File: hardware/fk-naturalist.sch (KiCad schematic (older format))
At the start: 133 parts, among them J1 Conn_01x11, J10 S2B-PH-SM4-TB, J11 RF-SMA-EDGE, J2 Conn_01x05, J3 Conn_01x04, J5 Conn_01x03, J6 Conn_01x05, J7 CONN-HDR-2x5, J8 Conn_01x09, J9 MICRO-USB, M1 MOUNT_HOLE, M3 MOUNT_HOLE, M4 MOUNT_HOLE, M6 MOUNT_HOLE, M7 MICROSD, Q1 2N7002LT1G, Q2 2N7002LT1G, Q3 2N7002LT1G, Q4 2N7002LT1G, SW1 SPNO, SW2 SPNO, U1 ATWINC1500-MR210PA, U10 FGPMMOPA6H, U101 TSL2591, U102 MPL3115A2, U103 BNO055, U104 SHT31, U11 MAX1704XX, U2 ATSAMD21G18A-AU, U3 SPH0645, U4 24AA02E64, U5 S25FL116K0XMFI041, U6 BQ24074RGTT, U7 PCF8523, U8 MCP1700T-3302E/MB, U9 ISL8541x, Y1 FC-135, Y101 FC-135, Y2 FC-135

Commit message: Fix TSL2591 footprint.
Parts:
- U101: footprint Housings_DFN_QFN:DFN-6-1EP_2x2mm_Pitch0.65mm -> conservify:TSL2591
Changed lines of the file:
@@
 F 0 "U101" H 9150 15300 60  0000 C CNN
 F 1 "TSL2591" H 9150 15400 60  0000 C CNN
-F 2 "Housings_DFN_QFN:DFN-6-1EP_2x2mm_Pitch0.65mm" H 9150 15300 60  0001 C CNN
+F 2 "conservify:TSL2591" H 9150 15300 60  0001 C CNN
 F 3 "" H 9150 15300 60  0001 C CNN
 F 4 "0" H 9150 15400 50  0001 C CNN "price"

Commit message: More label/naming cleanup.
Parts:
- C10, C19, C20, C25: value 4.7uF 10V X5R -> 4.7uF
- C12: value 1uF 50V X5R -> 1uF
- C14: value 4.7nF 25V X7R -> 4.7nF
- C21, C23, C27, C29, C6: value 1uF 10V X5R -> 1uF
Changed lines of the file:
@@
 P 5550 1900
 F 0 "C6" V 5400 1850 50  0000 L CNN
-F 1 "1uF 10V X5R" V 5700 1650 50  0000 L CNN
+F 1 "1uF" V 5700 1650 50  0000 L CNN
 F 2 "RocketScreamKicadLibrary:CAP-0603" H 5550 1700 30  0001 C CNN
 F 3 "" H 5550 1900 60  0000 C CNN
@@
 P 9100 2500
 F 0 "C12" H 9250 2500 50  0000 L CNN
-F 1 "1uF 50V X5R" H 9200 2600 50  0000 L CNN
+F 1 "1uF" H 9200 2600 50  0000 L CNN
 F 2 "RocketScreamKicadLibrary:CAP-0603" H 9100 2300 30  0001 C CNN
 F 3 "" H 9100 2500 60  0000 C CNN
@@
 P 12050 3000
 F 0 "C19" H 12100 3100 50  0000 L CNN
-F 1 "4.7uF 10V X5R" V 11900 2650 50  0000 L CNN
+F 1 "4.7uF" V 11900 2650 50  0000 L CNN
 F 2 "RocketScreamKicadLibrary:CAP-0603" H 12050 2800 30  0001 C CNN
 F 3 "" H 12050 3000 60  0000 C CNN
@@
 P 13000 2500
 F 0 "C20" H 13100 2500 50  0000 L CNN
-F 1 "4.7uF 10V X5R" H 13050 2400 50  0000 L CNN
+F 1 "4.7uF" H 13050 2400 50  0000 L CNN
 F 2 "RocketScreamKicadLibrary:CAP-0603" H 13000 2300 30  0001 C CNN
 F 3 "" H 13000 2500 60  0000 C CNN
@@
 P 14300 2500
 F 0 "C21" H 14050 2500 50  0000 L CNN
-F 1 "1uF 10V X5R" H 13700 2400 50  0000 L CNN
+F 1 "1uF" H 13700 2400 50  0000 L CNN
 F 2 "RocketScreamKicadLibrary:CAP-0603" H 14300 2300 30  0001 C CNN
 F 3 "" H 14300 2500 60  0000 C CNN
@@
 P 15200 2500
 F 0 "C23" H 15300 2500 50  0000 L CNN
-F 1 "1uF 10V X5R" H 15250 2400 50  0000 L CNN
+F 1 "1uF" H 15250 2400 50  0000 L CNN
 F 2 "RocketScreamKicadLibrary:CAP-0603" H 15200 2300 30  0001 C CNN
 F 3 "" H 15200 2500 60  0000 C CNN
@@
 P 11050 7000
 F 0 "C14" H 10800 7000 50  0000 L CNN
-F 1 "4.7nF 25V X7R" H 10400 6900 50  0000 L CNN
+F 1 "4.7nF" H 10400 6900 50  0000 L CNN
 F 2 "RocketScreamKicadLibrary:CAP-0603" H 11050 6800 30  0001 C CNN
 F 3 "" H 11050 7000 60  0000 C CNN
@@
 P 7500 6500
 F 0 "C10" H 7650 6500 50  0000 L CNN
-F 1 "4.7uF 10V X5R" H 7600 6400 50  0000 L CNN
+F 1 "4.7uF" H 7600 6400 50  0000 L CNN
 F 2 "RocketScreamKicadLibrary:CAP-0603" H 7500 6300 30  0001 C CNN
 F 3 "" H 7500 6500 60  0000 C CNN
@@
 P 18850 9550
 F 0 "C27" H 18900 9650 50  0000 L CNN
-F 1 "1uF 10V X5R" V 18700 9200 50  0000 L CNN
+F 1 "1uF" V 18700 9200 50  0000 L CNN
 F 2 "RocketScreamKicadLibrary:CAP-0603" H 18850 9350 30  0001 C CNN
 F 3 "" H 18850 9550 60  0000 C CNN
@@
 P 16800 3100
 F 0 "C25" H 16850 3200 50  0000 L CNN
-F 1 "4.7uF 10V X5R" V 16650 2750 50  0000 L CNN
+F 1 "4.7uF" V 16650 2750 50  0000 L CNN
 F 2 "RocketScreamKicadLibrary:CAP-0603" H 16800 2900 30  0001 C CNN
 F 3 "" H 16800 3100 60  0000 C CNN
@@
 P 20300 2750
 F 0 "C29" H 20400 2750 50  0000 L CNN
-F 1 "1uF 10V X5R" H 20350 2650 50  0000 L CNN
+F 1 "1uF" H 20350 2650 50  0000 L CNN
 F 2 "RocketScreamKicadLibrary:CAP-0603" H 20300 2550 30  0001 C CNN
 F 3 "" H 20300 2750 60  0000 C CNN

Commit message: Fix USB footprint with oval drills.
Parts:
- J9: footprint RocketScreamKicadLibrary:MICRO-USB -> conservify:MICRO-USB
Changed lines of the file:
@@
 F 0 "J9" H 10550 6800 60  0000 C CNN
 F 1 "MICRO-USB" H 10550 6100 60  0000 C CNN
-F 2 "RocketScreamKicadLibrary:MICRO-USB" H 10550 6000 60  0001 C CNN
+F 2 "conservify:MICRO-USB" H 10550 6000 60  0001 C CNN
 F 3 "" H 10600 6650 60  0000 C CNN
 F 4 "0.7" H 10550 6900 50  0001 C CNN "price"

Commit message: Adding peripheral enable NFET.
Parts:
- added J4: Conn_01x02, conservify:SJ_OPEN, symbol Conn_01x02
- added Q5: 2N7002LT1G, RocketScreamKicadLibrary:SOT-23, symbol MOSFET-N
- added R6: 10K, RocketScreamKicadLibrary:RES-0603, symbol RESISTOR
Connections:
- net labels added: PERIPH_ENABLE, PERIPH_GND
- wire segments 488 -> 500
- no-connect marks 38 -> 37
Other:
- note added: "PERIPHERALS"

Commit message: Adding some part numbers.
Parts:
- C104, C22, C24: spn1 81-GRM188R60J106ME47 -> 963-LMK107BBJ106KALT
- C14: spn1 603-AC603KRX7R8BB472 -> 80-C0603C472K9R
- C21, C23, C27, C29, C6: spn1 581-0603YD105K -> 963-UMK107BJ105KA-T
- R42, R43: spn1 (none) -> 603-AF0603JR-074K7L
- U3: spn1 (none) -> 721-SPH0645LM4H-B; supplier1 (none) -> mouser
- U9: spn1 (none) -> 968-ISL85415FRZ; supplier1 (none) -> mouser

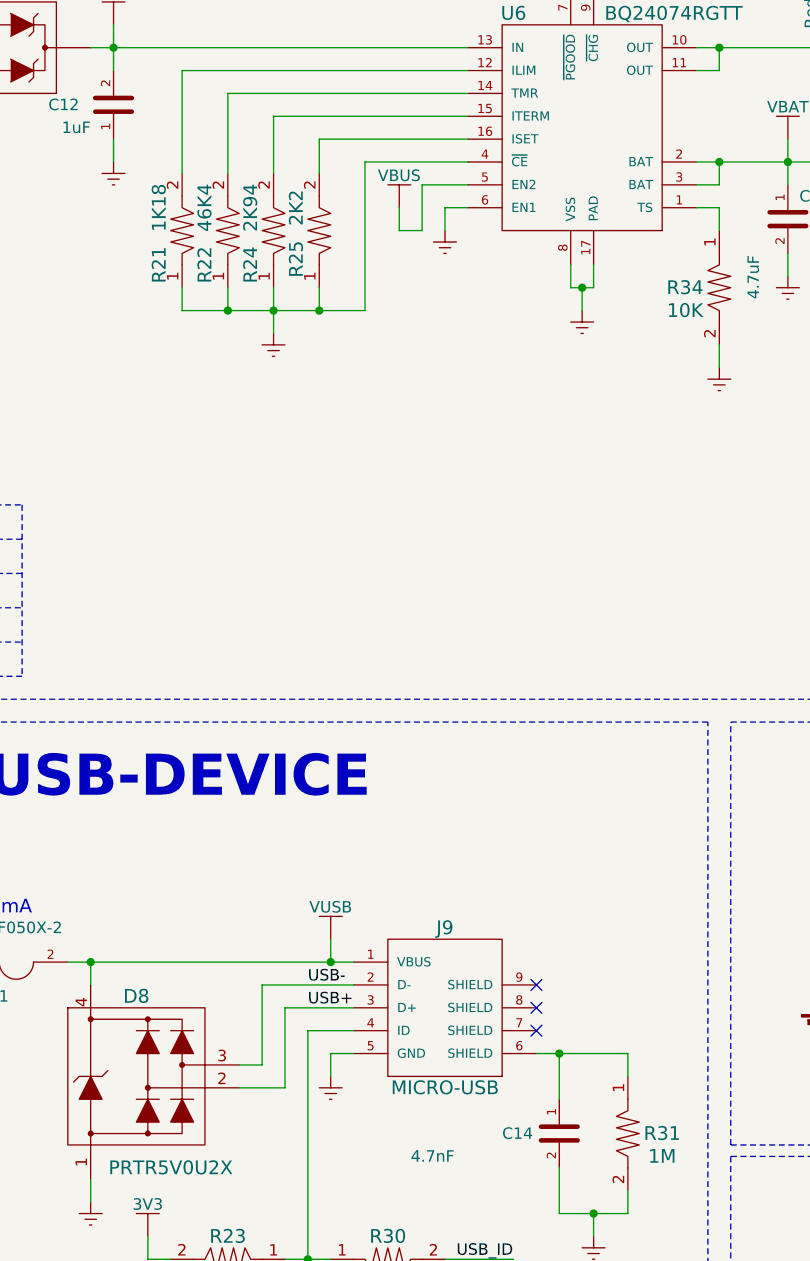
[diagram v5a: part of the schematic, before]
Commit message: Widen gap between USB and SD. Nudge USB out.
Giovanni recommended we make these changes to ease our enclosure design.
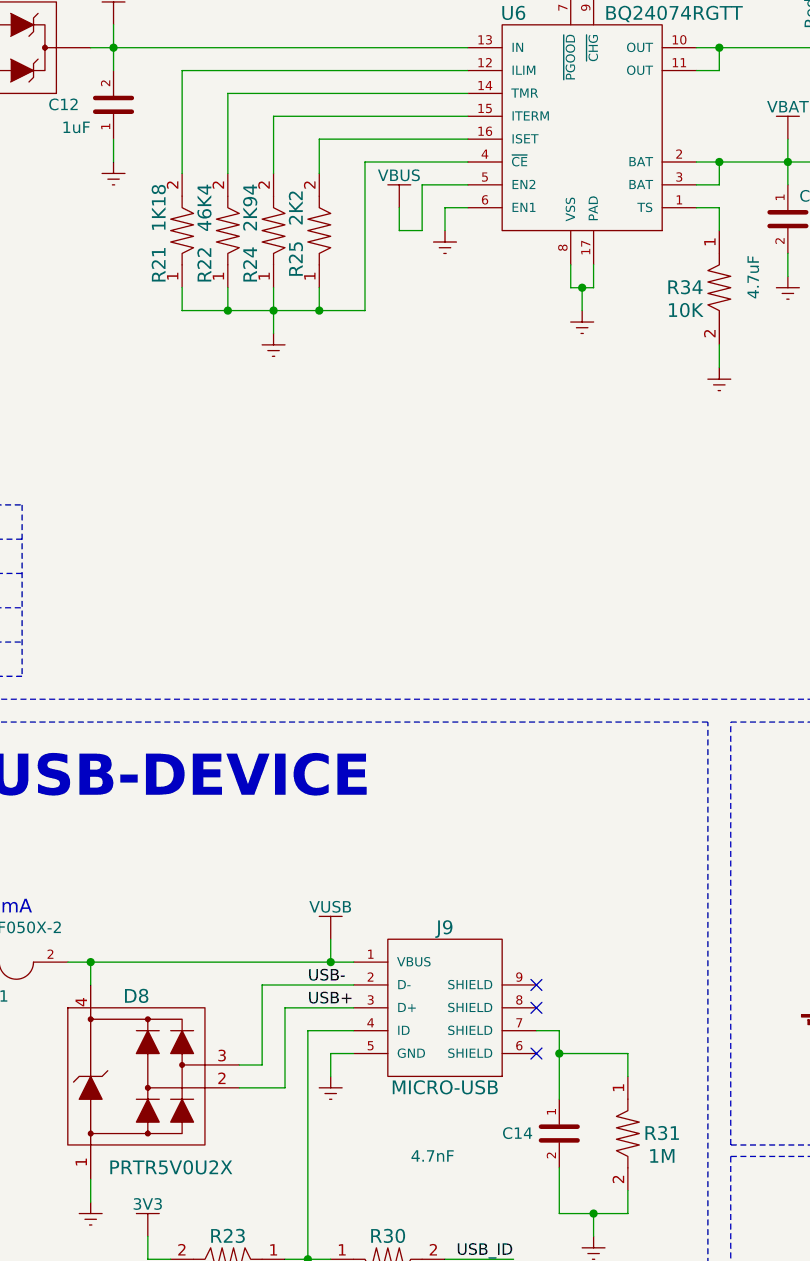
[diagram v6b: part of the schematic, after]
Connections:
- wire segments 500 -> 501
